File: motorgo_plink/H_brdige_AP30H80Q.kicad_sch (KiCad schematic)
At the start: 13 parts, among them J8 Conn_01x02_Pin, U4 DRV8874PWPR

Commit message: WIP - adding P/Ns to BOM (TS). will finish in afternoon.
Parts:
- C7, C8: LCSC_Part_Number (none) -> C3012377
- C9: footprint Capacitor_SMD:C_0402_1005Metric -> Capacitor_SMD:C_0201_0603Metric; Field4 (none) -> updated footprint TS 5-31-24; LCSC_Part_Number (none) -> C5142560
- J8: LCSC_Part_Number (none) -> C7430358
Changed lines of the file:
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@@
       (effects (font (size 1.27 1.27)) hide)
     )
-    (property "Datasheet" "~" (at 163.83 102.235 0)
+    (property "Datasheet" "https://www.lcsc.com/product-detail/Multilayer-Ceramic-Capacitors-MLCC-SMD-SMT_HRE-CSA0402X7R104K500GT_C3012377.html" (at 163.83 102.235 0)
+      (effects (font (size 1.27 1.27)) hide)
+    )
+    (property "LCSC_Part_Number" "C3012377" (at 163.83 102.235 0)
       (effects (font (size 1.27 1.27)) hide)
     )
@@
       (effects (font (size 1.27 1.27)) hide)
     )
-    (property "Datasheet" "~" (at 163.83 97.155 0)
+    (property "Datasheet" "https://www.lcsc.com/product-detail/Multilayer-Ceramic-Capacitors-MLCC-SMD-SMT_HRE-CSA0402X7R104K500GT_C3012377.html" (at 163.83 97.155 0)
+      (effects (font (size 1.27 1.27)) hide)
+    )
+    (property "LCSC_Part_Number" "C3012377" (at 163.83 97.155 0)
       (effects (font (size 1.27 1.27)) hide)
     )
@@
       (effects (font (size 1.27 1.27)) (justify left))
     )
-    (property "Footprint" "Capacitor_SMD:C_0402_1005Metric" (at 170.815 89.535 0)
-      (effects (font (size 1.27 1.27)) hide)
-    )
-    (property "Datasheet" "~" (at 170.815 89.535 0)
+    (property "Footprint" "Capacitor_SMD:C_0201_0603Metric" (at 170.815 89.535 0)
+      (effects (font (size 1.27 1.27)) hide)
+    )
+    (property "Datasheet" "https://www.lcsc.com/product-detail/Multilayer-Ceramic-Capacitors-MLCC-SMD-SMT_CCTC-TCC0201X5R223K250ZT_C5142560.html" (at 170.815 89.535 0)
+      (effects (font (size 1.27 1.27)) hide)
+    )
+    (property "Field4" "updated footprint TS 5-31-24" (at 170.815 89.535 0)
+      (effects (font (size 1.27 1.27)) hide)
+    )
+    (property "LCSC_Part_Number" "C5142560" (at 170.815 89.535 0)
       (effects (font (size 1.27 1.27)) hide)
     )
@@
       (effects (font (size 1.27 1.27)) hide)
     )
-    (property "Datasheet" "~" (at 188.595 128.905 0)
-      (effects (font (size 1.27 1.27)) hide)
-    )
+    (property "Datasheet" "https://www.lcsc.com/product-detail/Pin-Headers_CONNFLY-Elec-DS1021-1x2SF11-B_C7430358.html" (at 188.595 128.905 0)
+      (effects (font (size 1.27 1.27)) hide)
+    )
+    (property "LCSC_Part_Number" "C7430358" (at 188.595 128.905 0)
+      (effects (font (size 1.27 1.27)) hide)
+    )

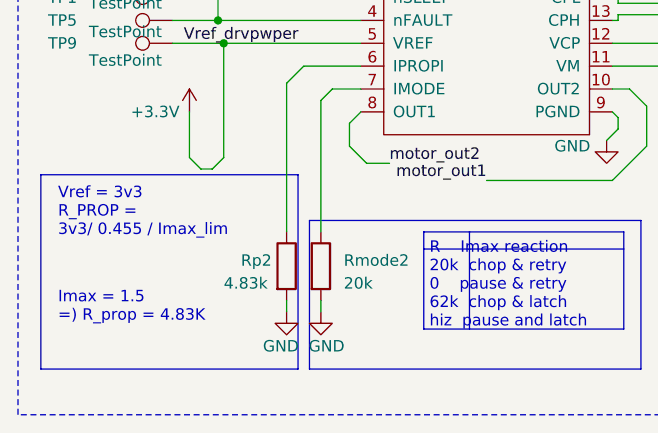
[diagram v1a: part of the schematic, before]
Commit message: finished first pass on BOM. check 100uF cap and a couple others. TS
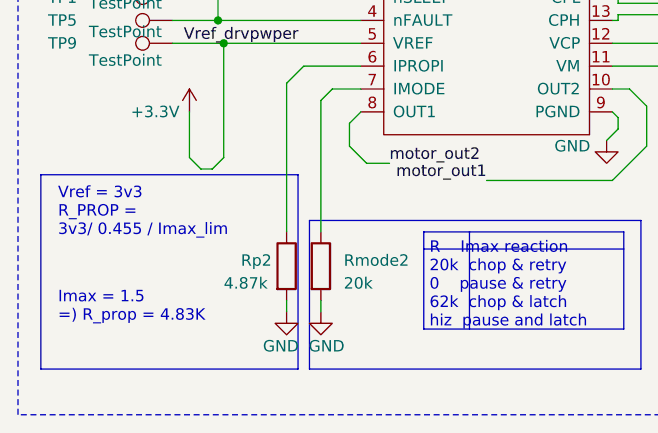
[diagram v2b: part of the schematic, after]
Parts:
- C10: Field4 (none) -> pending review for fit (TS) 5-31-24; LCSC_Part_Number (none) -> C141426
- R12, R13: LCSC_Part_Number (none) -> C2906885
- Rmode2: LCSC_Part_Number (none) -> C3017501
- Rp2: value 4.83k -> 4.87k; Field4 (none) -> updated to 4.87K from 4.83K. Confirmed 5-31-24 (TS); LCSC_Part_Number (none) -> C3015971
- U4: LCSC_Part_Number (none) -> C1855818
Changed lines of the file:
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@@
       (effects (font (size 1.27 1.27)) hide)
     )
-    (property "Datasheet" "https://www.lcsc.com/datasheet/lcsc_datasheet_2302221400_Texas-Instruments-DRV8874PWPR_C1855818.pdf" (at 141.605 87.503 0)
+    (property "Datasheet" "https://www.lcsc.com/product-detail/Motor-Driver-ICs_Texas-Instruments-DRV8874PWPR_C1855818.html" (at 141.605 87.503 0)
       (effects (font (size 1.27 1.27)) hide)
     )
@@
     )
     (property "uuid" "std:7384bdd1e05a4b1a8e1bd8e8948bd536" (at 141.605 92.583 0)
+      (effects (font (size 1.27 1.27)) hide)
+    )
+    (property "LCSC_Part_Number" "C1855818" (at 141.605 92.71 0)
       (effects (font (size 1.27 1.27)) hide)
     )
@@
       (effects (font (size 1.27 1.27)) hide)
     )
-    (property "Datasheet" "~" (at 166.37 76.835 0)
+    (property "Datasheet" "https://www.lcsc.com/product-detail/Chip-Resistor-Surface-Mount_FOJAN-FRC0402J103-TS_C2906885.html" (at 166.37 76.835 0)
+      (effects (font (size 1.27 1.27)) hide)
+    )
+    (property "LCSC_Part_Number" "C2906885" (at 166.37 76.835 0)
       (effects (font (size 1.27 1.27)) hide)
     )
@@
       (effects (font (size 1.27 1.27)) (justify left))
     )
-    (property "Value" "4.83k" (at 112.395 121.92 0)
+    (property "Value" "4.87k" (at 112.395 121.92 0)
       (effects (font (size 1.27 1.27)) (justify left))
     )
@@
       (effects (font (size 1.27 1.27)) hide)
     )
-    (property "Datasheet" "~" (at 119.38 120.015 0)
+    (property "Datasheet" "https://www.lcsc.com/product-detail/Chip-Resistor-Surface-Mount_VO-SCR0402F4K87_C3015971.html" (at 119.38 120.015 0)
+      (effects (font (size 1.27 1.27)) hide)
+    )
+    (property "Field4" "updated to 4.87K from 4.83K. Confirmed 5-31-24 (TS)" (at 119.38 120.015 0)
+      (effects (font (size 1.27 1.27)) hide)
+    )
+    (property "LCSC_Part_Number" "C3015971" (at 119.38 120.015 0)
       (effects (font (size 1.27 1.27)) hide)
     )
@@
       (effects (font (size 1.27 1.27)) hide)
     )
-    (property "Datasheet" "~" (at 177.165 104.775 0)
+    (property "Datasheet" "https://www.lcsc.com/product-detail/Aluminum-Electrolytic-Capacitors-SMD_ROQANG-VT1E101M0607_C141426.html" (at 177.165 104.775 0)
+      (effects (font (size 1.27 1.27)) hide)
+    )
+    (property "Field4" "pending review for fit (TS) 5-31-24 " (at 177.165 104.775 0)
+      (effects (font (size 1.27 1.27)) hide)
+    )
+    (property "LCSC_Part_Number" "C141426" (at 177.165 104.775 0)
       (effects (font (size 1.27 1.27)) hide)
     )
@@
       (effects (font (size 1.27 1.27)) hide)
     )
-    (property "Datasheet" "~" (at 111.76 83.82 0)
+    (property "Datasheet" "https://www.lcsc.com/product-detail/Chip-Resistor-Surface-Mount_FOJAN-FRC0402J103-TS_C2906885.html" (at 111.76 83.82 0)
+      (effects (font (size 1.27 1.27)) hide)
+    )
+    (property "LCSC_Part_Number" "C2906885" (at 111.76 83.82 0)
       (effects (font (size 1.27 1.27)) hide)
     )
@@
       (effects (font (size 1.27 1.27)) hide)
     )
-    (property "Datasheet" "~" (at 123.19 120.015 0)
-      (effects (font (size 1.27 1.27)) hide)
-    )
+    (property "Datasheet" "https://www.lcsc.com/product-detail/Chip-Resistor-Surface-Mount_VO-SCR0402J20K_C3017501.html" (at 123.19 120.015 0)
+      (effects (font (size 1.27 1.27)) hide)
+    )
+    (property "LCSC_Part_Number" "C3017501" (at 123.19 120.015 0)
+      (effects (font (size 1.27 1.27)) hide)
+    )

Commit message: swap electrolytic with MLCC cap. TS
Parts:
- C10: Field4 pending review for fit (TS) 5-31-24 -> go with MLCC for now; LCSC_Part_Number C141426 -> C6120014
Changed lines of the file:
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@@
       (effects (font (size 1.27 1.27)) hide)
     )
-    (property "Datasheet" "https://www.lcsc.com/product-detail/Aluminum-Electrolytic-Capacitors-SMD_ROQANG-VT1E101M0607_C141426.html" (at 177.165 104.775 0)
+    (property "Datasheet" "https://www.lcsc.com/product-detail/Multilayer-Ceramic-Capacitors-MLCC-SMD-SMT_HRE-CGA1210X5R107M160RT_C6120014.html" (at 177.165 104.775 0)
       (effects (font (size 1.27 1.27)) hide)
     )
-    (property "Field4" "pending review for fit (TS) 5-31-24 " (at 177.165 104.775 0)
+    (property "Field4" "go with MLCC for now" (at 177.165 104.775 0)
       (effects (font (size 1.27 1.27)) hide)
     )
-    (property "LCSC_Part_Number" "C141426" (at 177.165 104.775 0)
+    (property "LCSC_Part_Number" "C6120014" (at 177.165 104.775 0)
       (effects (font (size 1.27 1.27)) hide)
     )
